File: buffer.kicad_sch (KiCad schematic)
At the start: 7 parts, among them J16 V_SIG, J17 Conn_01x02_Pin, J18 VSIG_BUF, U6 BUF602xD

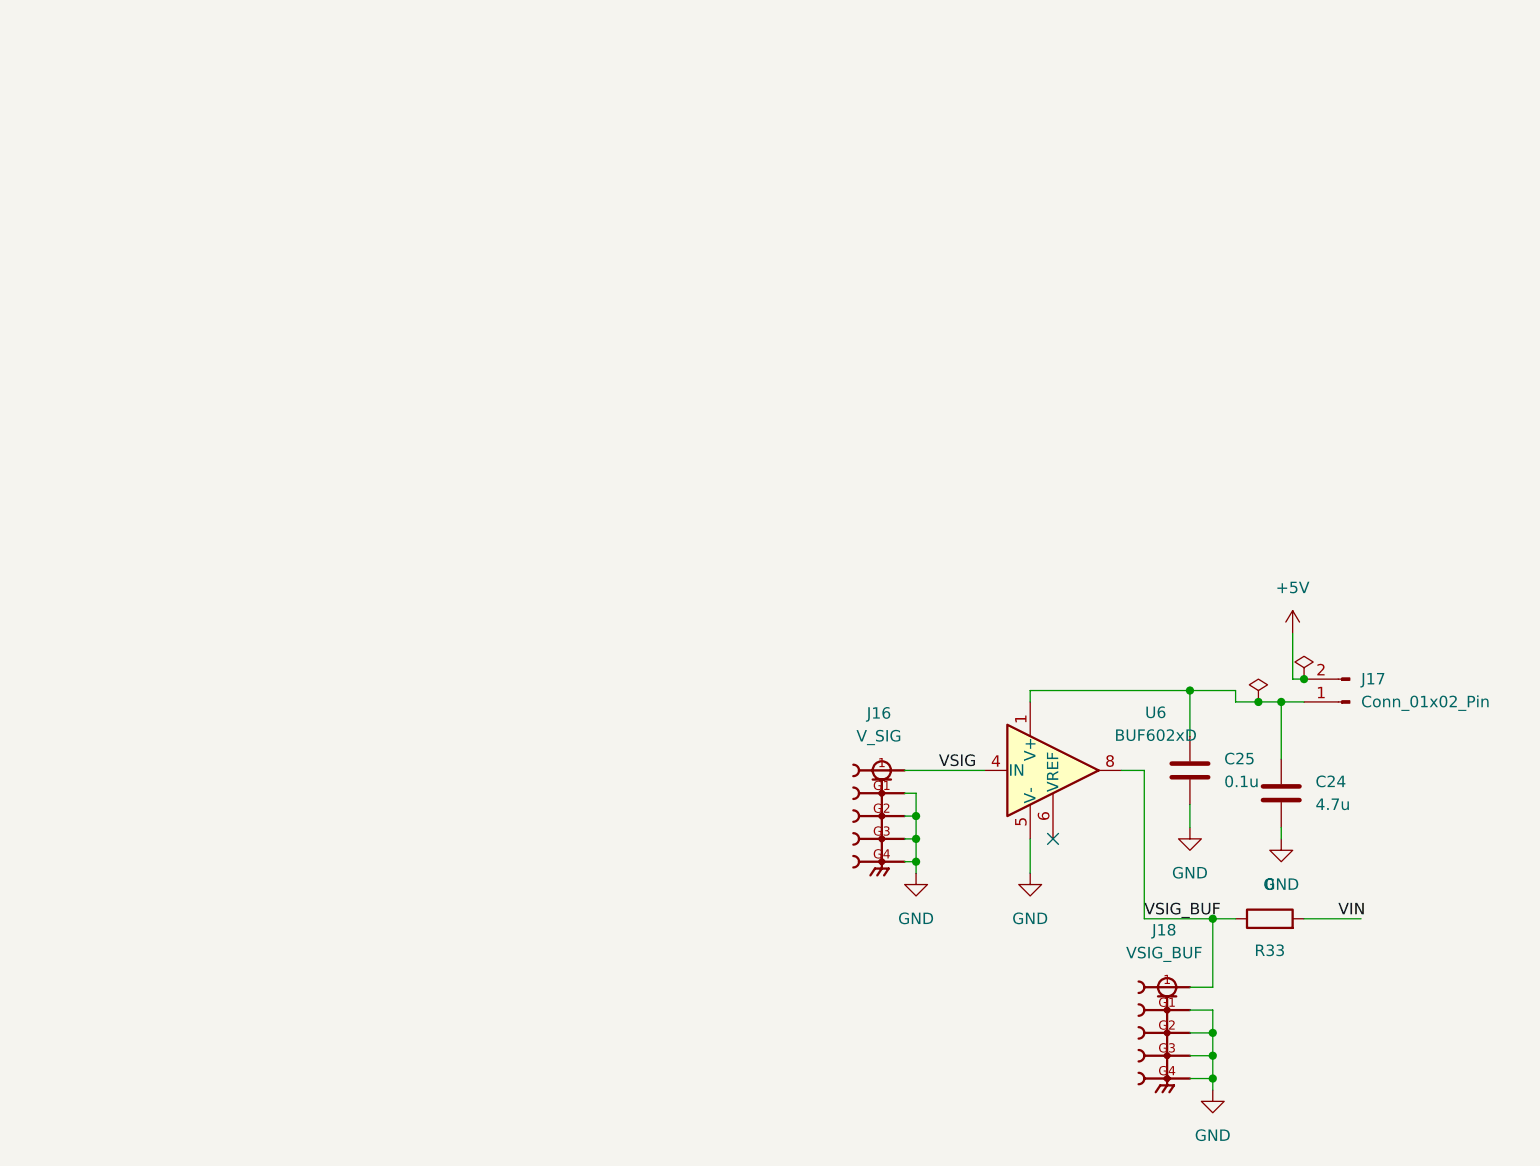
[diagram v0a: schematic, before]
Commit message: Finish the BUF602 buffer, add M3 mounting holes, direct-couple the SMAs
The netlist goes from 114 parts and 89 nets to 116 parts and 84 nets.
ERC shows 0 errors and 37 warnings.

Schematic edits by Luke
- Buffer sheet. ls1031's J16, J17 and J18 removed. The BUF602 (U6) now
  uses the top-sheet SMAs, J13 on its input (VSIG) and J14 on its output
  (VSIG_BUF, was J15), both now the edge-mount Samtec part. Its output
  reaches the chip's VDD pins through R34 (2.2 ohm) onto SHUNT_IN_B. V+
  comes from +5V through jumper J12 BUF_EN.
- The buffer's supply caps renumbered to C26 (4.7u) and C27 (0.1u), so
  C24 and C25 are the INA190 input filter caps again.
- C8 and C10 removed. J5 now connects directly to SHUNT_IN_B (VDD_LDO)
  and J6 directly to SHUNT_OUT_A (VOUT_LDO).
- Four mounting holes, H1 to H4.

Field edits by Claude
- U6 is the TI BUF602ID (tube; the BUF602IDR reel is obsolete at DigiKey).
- R34 footprint and part, Panasonic ERJ-6RQF2R2V.
- C26 and C27 part numbers changed to match their values (they carried a
  10 uF 10 V KEMET number), Samsung CL21B475KAFNNNE and CL21B104KBCNNNC.
- H1 to H4 footprint changed from the 2-pin header to
  MountingHole_3.2mm_M3, per the guidelines' four M3 holes.
Netlist exports before and after each field edit have identical nets.

Co-Authored-By: Claude Opus 5.5 (1M context) <noreply@anthropic.com>
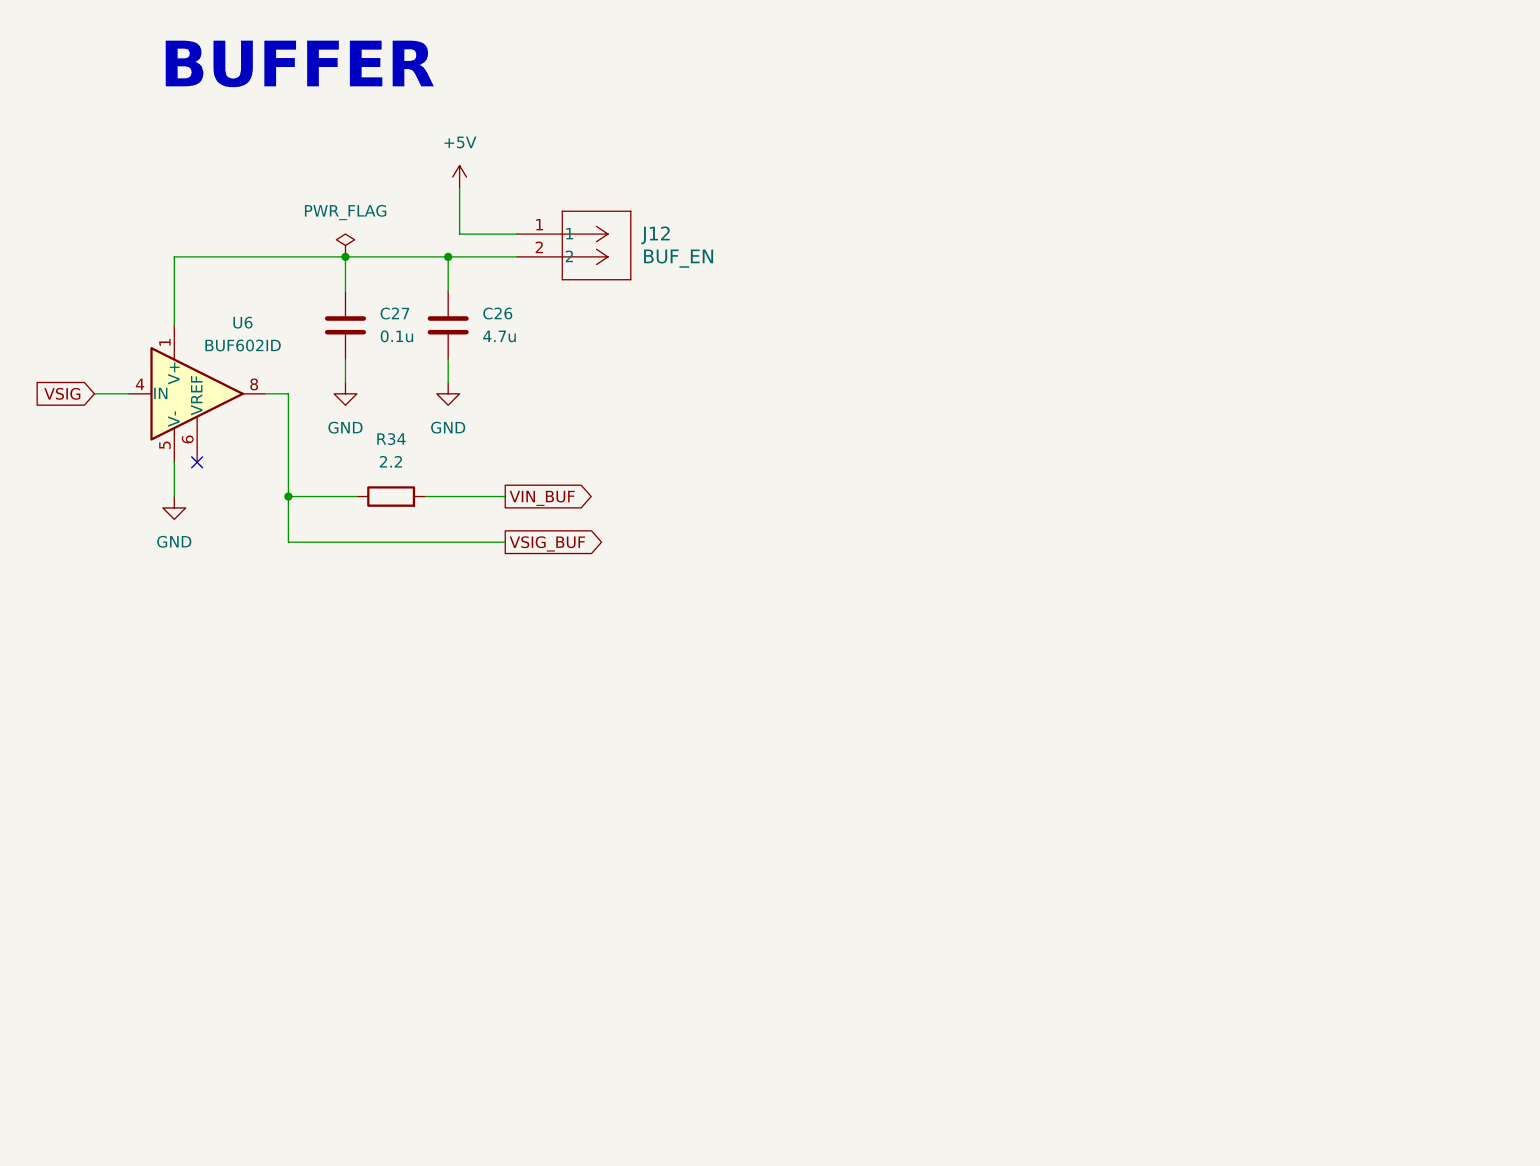
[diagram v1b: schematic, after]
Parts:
- removed C24: 4.7u, Capacitor_SMD:C_0805_2012Metric_Pad1.18x1.45mm_HandSolder, symbol Device:C
- removed C25: 0.1u, Capacitor_SMD:C_0805_2012Metric_Pad1.18x1.45mm_HandSolder, symbol Device:C
- removed J16: V_SIG, TPS7A7001_Evaluation_Board_footprint_lib:SAMTEC_SMA-J-P-H-ST-TH1, symbol SMA-J-P-H-ST-TH1:SMA-J-P-H-ST-TH1
- removed J17: Conn_01x02_Pin, Package_DIP:DIP-20_W7.62mm, symbol Connector:Conn_01x02_Pin
- removed J18: VSIG_BUF, SMA_J_P_H_ST_TH1:SAMTEC_SMA-J-P-H-ST-TH1, symbol SMA-J-P-H-ST-TH1:SMA-J-P-H-ST-TH1
- removed R33: 0, Resistor_SMD:R_0805_2012Metric_Pad1.20x1.40mm_HandSolder, symbol Device:R
- added C26: 4.7u, Capacitor_SMD:C_0805_2012Metric_Pad1.18x1.45mm_HandSolder, symbol Device:C
- added C27: 0.1u, Capacitor_SMD:C_0805_2012Metric_Pad1.18x1.45mm_HandSolder, symbol Device:C
- added J12: BUF_EN, ldo_bringup_board_ee372:CONN_PxC02S_SUL, symbol ldo_bringup_board_ee372:PEC02SAAN
- added R34: 2.2, Resistor_SMD:R_0805_2012Metric_Pad1.20x1.40mm_HandSolder, symbol Device:R
- U6: value BUF602xD -> BUF602ID; Distributer Link 1 (none) -> https://www.digikey.com/en/products/detail/texas-instrument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; Manufacturer (none) -> Texas Instruments; Manufacturer Part Number (none) -> BUF602ID
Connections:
- net +5V: now also J12.1
- net GND: now also C26.1, C27.1
- net VSIG_BUF: now also R34.1
- net at U6.1 (V+): now also C26.2, C27.2, J12.2
- new net VIN_BUF: R34.2
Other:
- note added: "BUFFER"
- title: (none) -> EE372 LDO bringup board
- moved on the sheet: U6
